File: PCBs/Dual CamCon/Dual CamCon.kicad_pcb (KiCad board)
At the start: 2 copper layers, 7 parts, among them J1 Servo Input, J2 Servo Input, J3 Camera FPC Connector, J4 Camera FPC Connector, J5 Raspberry Pi GPIO, P1 HDMI Connector, P2 HDMI Connector

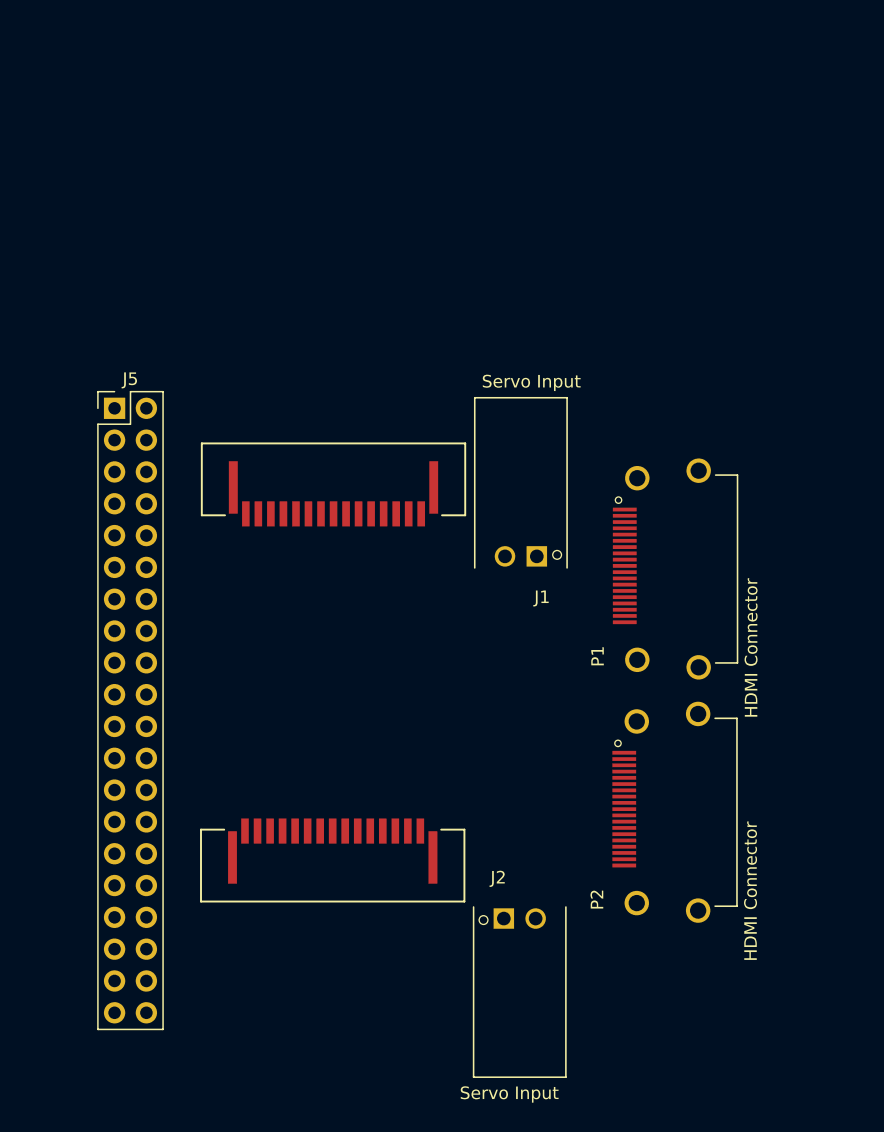
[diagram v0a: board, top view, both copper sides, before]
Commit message: Finished Mechanicals of the Dual CamCon Board
Just need to do the routing now.
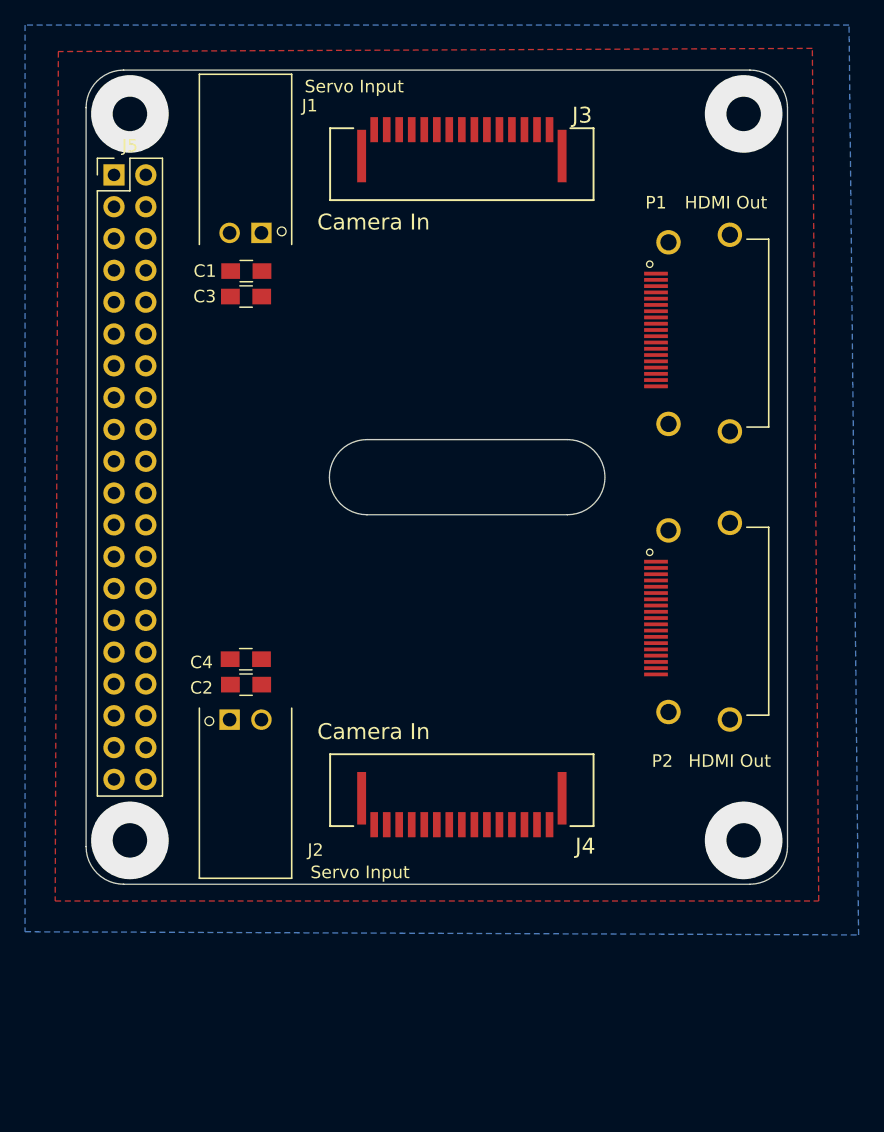
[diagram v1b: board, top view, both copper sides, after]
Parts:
- added C1: , EER:C_0805_HandSoldering, F.Cu at (112.8, 51.0)
- added C2: , EER:C_0805_HandSoldering, F.Cu at (112.8, 84.1)
- added C3: , EER:C_0805_HandSoldering, F.Cu at (112.8, 53.1)
- added C4: , EER:C_0805_HandSoldering, F.Cu at (112.8, 82.0)
- J3, J4: value Camera FPC Connector -> Camera In
- P1, P2: value HDMI Connector -> HDMI Out
- moved J3 37.6 mm to (130.0, 37.0), turned to 180 degrees
- moved J1 33.9 mm to (114.0, 48.0)
- moved J2 27.0 mm to (111.5, 86.9)
- moved P1 19.0 mm to (145.5, 56.0)
- moved J5 18.6 mm to (102.2, 43.4)
- moved P2 15.5 mm to (145.5, 79.0)
- moved J4 11.5 mm to (130.0, 98.0), turned to 0 degrees
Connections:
- J1 pad 1: Net-(J1-Pad1) -> GND
- J1 pad 2: Net-(J1-Pad2) -> /Servo1
- J2 pad 1: Net-(J2-Pad1) -> GND
- J2 pad 2: Net-(J2-Pad2) -> /Servo2
- J3 pad 1: Net-(J3-Pad1) -> GND
- J3 pad 10: Net-(J3-Pad10) -> GND
- J3 pad 11: Net-(J3-Pad11) -> /CAM1_GPIO
- J3 pad 12: Net-(J3-Pad12) -> /CAM1_CLK
- J3 pad 13: Net-(J3-Pad13) -> /CAM1_SCL
- J3 pad 14: Net-(J3-Pad14) -> /CAM1_SDA
- J3 pad 15: Net-(J3-Pad15) -> /CAM1_3V3
- J3 pad 16: Net-(J3-Pad16) -> GND
- J3 pad 17: Net-(J3-Pad17) -> GND
- J3 pad 2: Net-(J3-Pad2) -> /CAM1_DN0
- J3 pad 3: Net-(J3-Pad3) -> /CAM1_DP0
- J3 pad 4: Net-(J3-Pad4) -> GND
- J3 pad 5: Net-(J3-Pad5) -> /CAM1_DN1
- J3 pad 6: Net-(J3-Pad6) -> /CAM1_DP1
- J3 pad 7: Net-(J3-Pad7) -> GND
- J3 pad 8: Net-(J3-Pad8) -> /CAM1_CN
- J3 pad 9: Net-(J3-Pad9) -> /CAM1_CP
- J4 pad 1: Net-(J4-Pad1) -> GND
- J4 pad 10: Net-(J4-Pad10) -> GND
- J4 pad 11: Net-(J4-Pad11) -> /CAM2_GPIO
- J4 pad 12: Net-(J4-Pad12) -> /CAM2_CLK
- J4 pad 13: Net-(J4-Pad13) -> /CAM2_SCL
- J4 pad 14: Net-(J4-Pad14) -> /CAM2_SDA
- J4 pad 15: Net-(J4-Pad15) -> /CAM2_3V3
- J4 pad 16: Net-(J4-Pad16) -> GND
- J4 pad 17: Net-(J4-Pad17) -> GND
- J4 pad 2: Net-(J4-Pad2) -> /CAM2_DN0
- J4 pad 3: Net-(J4-Pad3) -> /CAM2_DP0
- J4 pad 4: Net-(J4-Pad4) -> GND
- J4 pad 5: Net-(J4-Pad5) -> /CAM2_DN1
- J4 pad 6: Net-(J4-Pad6) -> /CAM2_DP1
- J4 pad 7: Net-(J4-Pad7) -> GND
- J4 pad 8: Net-(J4-Pad8) -> /CAM2_CN
- J4 pad 9: Net-(J4-Pad9) -> /CAM2_CP
- P1 pad 1: Net-(P1-Pad1) -> /CAM1_DN0
- P1 pad 10: Net-(P1-Pad10) -> /CAM1_GPIO
- P1 pad 11: Net-(P1-Pad11) -> GND
- P1 pad 12: Net-(P1-Pad12) -> /CAM1_CLK
- P1 pad 13: Net-(P1-Pad13) -> /CAM1_SCL
- P1 pad 14: Net-(P1-Pad14) -> /CAM1_SDA
- P1 pad 15: Net-(P1-Pad15) -> /CAM1_3V3
- P1 pad 16: Net-(P1-Pad16) -> /Servo1
- P1 pad 17: Net-(P1-Pad17) -> GND
- P1 pad 18: Net-(P1-Pad18) -> +5V
- P1 pad 19: Net-(P1-Pad19) -> +5V
- P1 pad 2: Net-(P1-Pad2) -> GND
- P1 pad 3: Net-(P1-Pad3) -> /CAM1_DP0
- P1 pad 4: Net-(P1-Pad4) -> /CAM1_DN1
- P1 pad 5: Net-(P1-Pad5) -> GND
- P1 pad 6: Net-(P1-Pad6) -> /CAM1_DP1
- P1 pad 7: Net-(P1-Pad7) -> /CAM1_CN
- P1 pad 8: Net-(P1-Pad8) -> GND
- P1 pad 9: Net-(P1-Pad9) -> /CAM1_CP
- P2 pad 1: Net-(P2-Pad1) -> /CAM2_DN0
- P2 pad 10: Net-(P2-Pad10) -> /CAM2_GPIO
- P2 pad 11: Net-(P2-Pad11) -> GND
- P2 pad 12: Net-(P2-Pad12) -> /CAM2_CLK
- P2 pad 13: Net-(P2-Pad13) -> /CAM2_SCL
- P2 pad 14: Net-(P2-Pad14) -> /CAM2_SDA
- P2 pad 15: Net-(P2-Pad15) -> /CAM2_3V3
- P2 pad 16: Net-(P2-Pad16) -> /Servo2
- P2 pad 17: Net-(P2-Pad17) -> GND
- P2 pad 18: Net-(P2-Pad18) -> +5V
- P2 pad 19: Net-(P2-Pad19) -> +5V
- P2 pad 2: Net-(P2-Pad2) -> GND
- P2 pad 3: Net-(P2-Pad3) -> /CAM2_DP0
- P2 pad 4: Net-(P2-Pad4) -> /CAM2_DN1
- P2 pad 5: Net-(P2-Pad5) -> GND
- P2 pad 6: Net-(P2-Pad6) -> /CAM2_DP1
- P2 pad 7: Net-(P2-Pad7) -> /CAM2_CN
- P2 pad 8: Net-(P2-Pad8) -> GND
- P2 pad 9: Net-(P2-Pad9) -> /CAM2_CP
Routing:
- net (no net): vias 0 -> 4
- added copper zone on B.Cu, net GND
- added copper zone on F.Cu, net GND
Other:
- board outline added: 56 x 65 mm

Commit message: Dual CamCon Board - Ready for Review
Pretty much cleaned up this guy as much as I could. Needs to be reviewed by the team on a few different things.

-FPC to HDMI legitness (will each pin line up) needs to be triple checked.
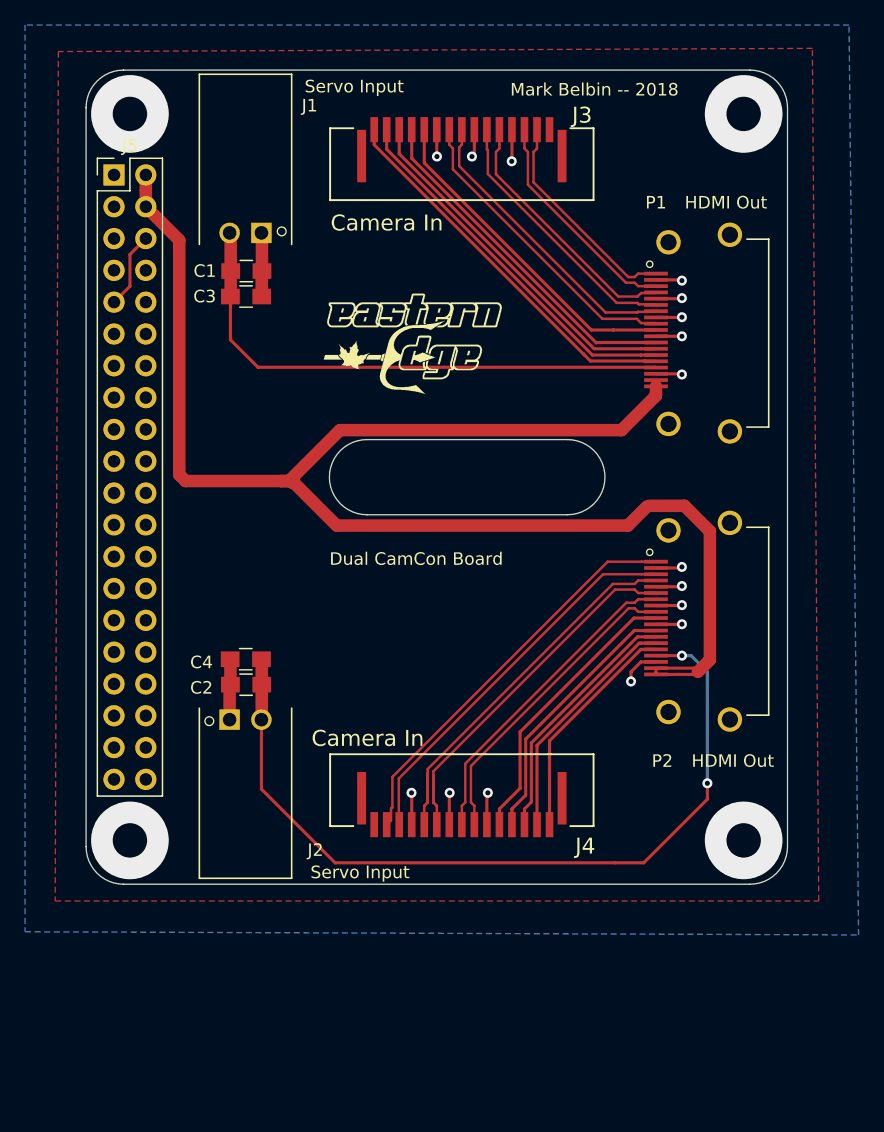
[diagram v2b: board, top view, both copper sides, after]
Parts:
- added ?: , EER:EERLOGO, F.Cu at (116.5, 62.6)
- added U$15: MUNLOGO, EER:MUNLOGO, B.Cu at (141.0, 85.8)
- added U$16: MILOGO, EER:MILOGO, B.Cu at (140.1, 59.8)
- C1, C2, C3, C4: value (none) -> C
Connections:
- net /CAM1_CN renamed /CAM1_C-
- net /CAM1_CP renamed /CAM1_C+
- net /CAM1_DN0 renamed /CAM1_D0-
- net /CAM1_DN1 renamed /CAM1_D1-
- net /CAM1_DP0 renamed /CAM1_D0+
- net /CAM1_DP1 renamed /CAM1_D1+
- net /CAM2_CN renamed /CAM2_C-
- net /CAM2_CP renamed /CAM2_C+
- net /CAM2_DN0 renamed /CAM2_D0-
- net /CAM2_DN1 renamed /CAM2_D1-
- net /CAM2_DP0 renamed /CAM2_D0+
- net /CAM2_DP1 renamed /CAM2_D1+
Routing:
- net +5V: track 0.00 -> 125.9 mm
- net /Servo2: track 0.00 -> 65.5 mm, vias 0 -> 2
- net GND: track 0.00 -> 52.6 mm, vias 0 -> 16
- net /Servo1: track 0.00 -> 43.5 mm
- net /CAM2_D0-: track 0.00 -> 32.7 mm
- net /CAM2_D1-: track 0.00 -> 31.8 mm
- net /CAM1_3V3: track 0.00 -> 31.0 mm
- net /CAM2_D0+: track 0.00 -> 31.0 mm
- net /CAM2_D1+: track 0.00 -> 30.8 mm
- net /CAM1_SDA: track 0.00 -> 29.9 mm
- net /CAM1_SCL: track 0.00 -> 28.9 mm
- net /CAM1_CLK: track 0.00 -> 27.9 mm
- net /CAM1_GPIO: track 0.00 -> 26.7 mm
- net /CAM2_C-: track 0.00 -> 25.6 mm
- net /CAM2_C+: track 0.00 -> 24.9 mm
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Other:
- net class Thicker added: clearance 0.2, trace_width 1, via_dia 0.8, via_drill 0.4
- rule via_min_size: 0.4 -> 0.3
- board text added: "Dual CamCon Board"
- board text added: "Mark Belbin -- 2018"

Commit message: Major Routing Fix for Dual CamCon
After looking at the physical Pi Cam I realized that I had the pin map mirrored. I swapped the pins around on the FPC connector and cleaned up the board in general. Count this as a double check, still need another check from someone else.
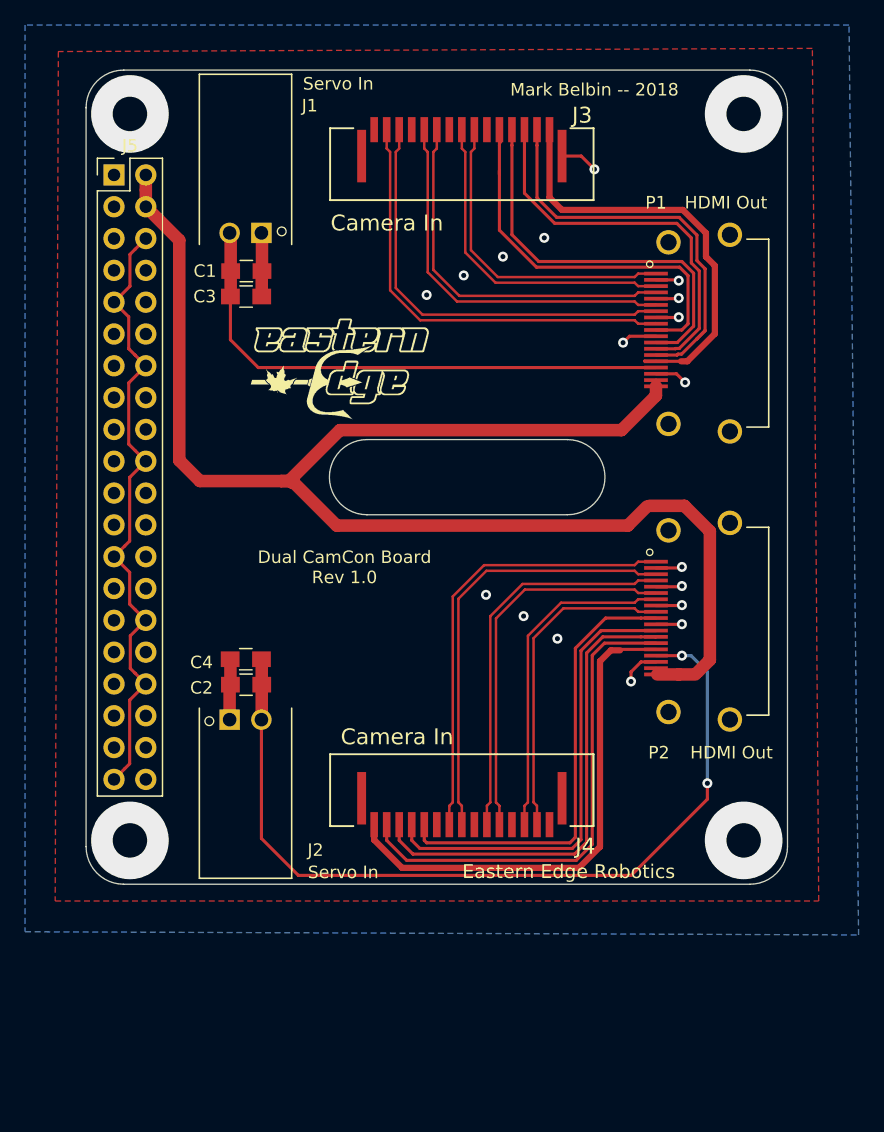
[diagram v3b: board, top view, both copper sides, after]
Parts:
- J1, J2: value Servo Input -> Servo In
- moved ? 6.16 mm to (110.6, 64.6)
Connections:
- J3 pad 1: GND -> /CAM1_3V3
- J3 pad 10: GND -> /CAM1_D1+
- J3 pad 11: /CAM1_GPIO -> /CAM1_D1-
- J3 pad 12: /CAM1_CLK -> GND
- J3 pad 13: /CAM1_SCL -> /CAM1_D0+
- J3 pad 14: /CAM1_SDA -> /CAM1_D0-
- J3 pad 15: /CAM1_3V3 -> GND
- J3 pad 2: /CAM1_D0- -> /CAM1_SDA
- J3 pad 3: /CAM1_D0+ -> /CAM1_SCL
- J3 pad 4: GND -> /CAM1_CLK
- J3 pad 5: /CAM1_D1- -> /CAM1_GPIO
- J3 pad 6: /CAM1_D1+ -> GND
- J3 pad 7: GND -> /CAM1_C+
- J3 pad 9: /CAM1_C+ -> GND
- J4 pad 1: GND -> /CAM2_3V3
- J4 pad 10: GND -> /CAM2_D1+
- J4 pad 11: /CAM2_GPIO -> /CAM2_D1-
- J4 pad 12: /CAM2_CLK -> GND
- J4 pad 13: /CAM2_SCL -> /CAM2_D0+
- J4 pad 14: /CAM2_SDA -> /CAM2_D0-
- J4 pad 15: /CAM2_3V3 -> GND
- J4 pad 2: /CAM2_D0- -> /CAM2_SDA
- J4 pad 3: /CAM2_D0+ -> /CAM2_SCL
- J4 pad 4: GND -> /CAM2_CLK
- J4 pad 5: /CAM2_D1- -> /CAM2_GPIO
- J4 pad 6: /CAM2_D1+ -> GND
- J4 pad 7: GND -> /CAM2_C+
- J4 pad 9: /CAM2_C+ -> GND
- P1 pad 1: /CAM1_D0- -> /CAM1_C+
- P1 pad 3: /CAM1_D0+ -> /CAM1_C-
- P1 pad 4: /CAM1_D1- -> /CAM1_D1+
- P1 pad 6: /CAM1_D1+ -> /CAM1_D1-
- P1 pad 7: /CAM1_C- -> /CAM1_D0+
- P1 pad 9: /CAM1_C+ -> /CAM1_D0-
- P1 pad P1: (no net) -> GND
- P1 pad P2: (no net) -> GND
- P1 pad P3: (no net) -> GND
- P1 pad P4: (no net) -> GND
- P2 pad 1: /CAM2_D0- -> /CAM2_C+
- P2 pad 3: /CAM2_D0+ -> /CAM2_C-
- P2 pad 4: /CAM2_D1- -> /CAM2_D1+
- P2 pad 6: /CAM2_D1+ -> /CAM2_D1-
- P2 pad 7: /CAM2_C- -> /CAM2_D0+
- P2 pad 9: /CAM2_C+ -> /CAM2_D0-
- P2 pad P1: (no net) -> GND
- P2 pad P2: (no net) -> GND
- P2 pad P3: (no net) -> GND
- P2 pad P4: (no net) -> GND
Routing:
- net GND: track 52.6 -> 86.8 mm, vias 16 -> 18
- net /CAM2_SDA: track 19.2 -> 40.0 mm
- net /CAM2_3V3: track 19.8 -> 40.5 mm
- net /CAM2_SCL: track 20.2 -> 38.3 mm
- net /CAM1_D0-: track 17.3 -> 35.3 mm
- net /CAM1_D0+: track 18.1 -> 34.6 mm
- net /CAM2_CLK: track 21.3 -> 37.1 mm
- net /CAM2_GPIO: track 22.7 -> 36.1 mm
- net /CAM2_C+: track 24.9 -> 35.7 mm
- net /CAM1_D1-: track 20.6 -> 30.9 mm
- net /CAM2_C-: track 25.6 -> 35.0 mm
- net /CAM1_D1+: track 21.3 -> 30.1 mm
- net /CAM2_D0-: track 32.7 -> 25.9 mm
- net /CAM1_GPIO: track 26.7 -> 32.5 mm
- net /CAM2_D0+: track 31.0 -> 26.6 mm
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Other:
- net class Thicker: trace_width 1 -> 0.5
- board text added: "Dual CamCon Board Rev 1.0"
- board text added: "Eastern Edge Robotics"
- board text removed: "Dual CamCon Board"

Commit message: Touched up Dual CamCon
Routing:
- net /CAM1_SDA: track 33.0 -> 32.0 mm
- net GND: vias 18 -> 86

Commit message: DC-DC Board Final
99% Done the first DC-DC Board. Just need to double check everything!!
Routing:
- net GND: vias 86 -> 87
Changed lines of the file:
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@@
     (thickness 1.6)
     (drawings 16)
-    (tracks 389)
+    (tracks 390)
     (zones 0)
     (modules 14)
@@
   (via (at 143.43046 89.64438) (size 0.8) (drill 0.4) (layers F.Cu B.Cu) (net 2))
   (via (at 127.48046 83.89438) (size 0.8) (drill 0.4) (layers F.Cu B.Cu) (net 2))
+  (via (at 147.78046 97.99438) (size 0.8) (drill 0.4) (layers F.Cu B.Cu) (net 2))
   (segment (start 104.77 44.572081) (end 104.77 45.91) (width 1) (layer F.Cu) (net 30))
   (segment (start 104.77 43.37) (end 104.77 44.572081) (width 1) (layer F.Cu) (net 30))
@@
   (segment (start 147.2 83.25) (end 147.31746 83.25) (width 0.25) (layer F.Cu) (net 30))
   (segment (start 147.31746 83.25) (end 148.64184 83.25) (width 1) (layer F.Cu) (net 30))
-  (segment (start 145.5 60.99184) (end 145.5 60.25) (width 1) (layer F.Cu) (net 30))
-  (segment (start 142.74546 63.74638) (end 145.5 60.99184) (width 1) (layer F.Cu) (net 30))
-  (segment (start 120.26646 63.74638) (end 142.74546 63.74638) (width 1) (layer F.Cu) (net 30))
-  (segment (start 115.56746 67.81038) (end 116.20246 67.81038) (width 1) (layer F.Cu) (net 30))
-  (segment (start 116.20246 67.81038) (end 120.26646 63.74638) (width 1) (layer F.Cu) (net 30))
-  (segment (start 143.25346 71.36638) (end 144.77746 69.84238) (width 1) (layer F.Cu) (net 30))
-  (segment (start 120.01246 71.36638) (end 143.25346 71.36638) (width 1) (layer F.Cu) (net 30))
-  (segment (start 116.58346 67.93738) (end 120.01246 71.36638) (width 1) (layer F.Cu) (net 30))
-  (segment (start 116.45646 67.93738) (end 116.58346 67.93738) (width 1) (layer F.Cu) (net 30))
-  (segment (start 115.56746 67.81038) (end 116.32946 67.81038) (width 1) (layer F.Cu) (net 30))
-  (segment (start 116.32946 67.81038) (end 116.45646 67.93738) (width 1) (layer F.Cu) (net 30))
   (segment (start 145.5 60.15) (end 145.5 59.75) (width 0.25) (layer F.Cu) (net 30))
   (segment (start 145.4 60.25) (end 145.5 60.15) (width 0.25) (layer F.Cu) (net 30))
@@
   (segment (start 104.77 45.91) (end 107.43946 48.57946) (width 1) (layer F.Cu) (net 30))
   (segment (start 107.43946 48.57946) (end 107.43946 66.15938) (width 1) (layer F.Cu) (net 30))
+  (segment (start 145.5 60.99184) (end 145.5 60.25) (width 1) (layer F.Cu) (net 30))
+  (segment (start 143.29746 63.19438) (end 145.5 60.99184) (width 1) (layer F.Cu) (net 30))
+  (segment (start 120.81846 63.19438) (end 143.29746 63.19438) (width 1) (layer F.Cu) (net 30))
+  (segment (start 115.56746 67.81038) (end 116.20246 67.81038) (width 1) (layer F.Cu) (net 30))
+  (segment (start 116.20246 67.81038) (end 120.81846 63.19438) (width 1) (layer F.Cu) (net 30))
+  (segment (start 142.67546 71.94438) (end 144.77746 69.84238) (width 1) (layer F.Cu) (net 30))
+  (segment (start 120.59046 71.94438) (end 142.67546 71.94438) (width 1) (layer F.Cu) (net 30))
+  (segment (start 116.58346 67.93738) (end 120.59046 71.94438) (width 1) (layer F.Cu) (net 30))
+  (segment (start 116.45646 67.93738) (end 116.58346 67.93738) (width 1) (layer F.Cu) (net 30))
+  (segment (start 115.56746 67.81038) (end 116.32946 67.81038) (width 1) (layer F.Cu) (net 30))
+  (segment (start 116.32946 67.81038) (end 116.45646 67.93738) (width 1) (layer F.Cu) (net 30))
   (segment (start 111.52346 56.52738) (end 111.52346 53.07838) (width 0.25) (layer F.Cu) (net 33))
   (segment (start 111.54346 53.05838) (end 111.52346 53.07838) (width 0.25) (layer F.Cu) (net 33))
